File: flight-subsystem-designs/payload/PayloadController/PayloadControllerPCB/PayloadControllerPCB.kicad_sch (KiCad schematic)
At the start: 2 parts

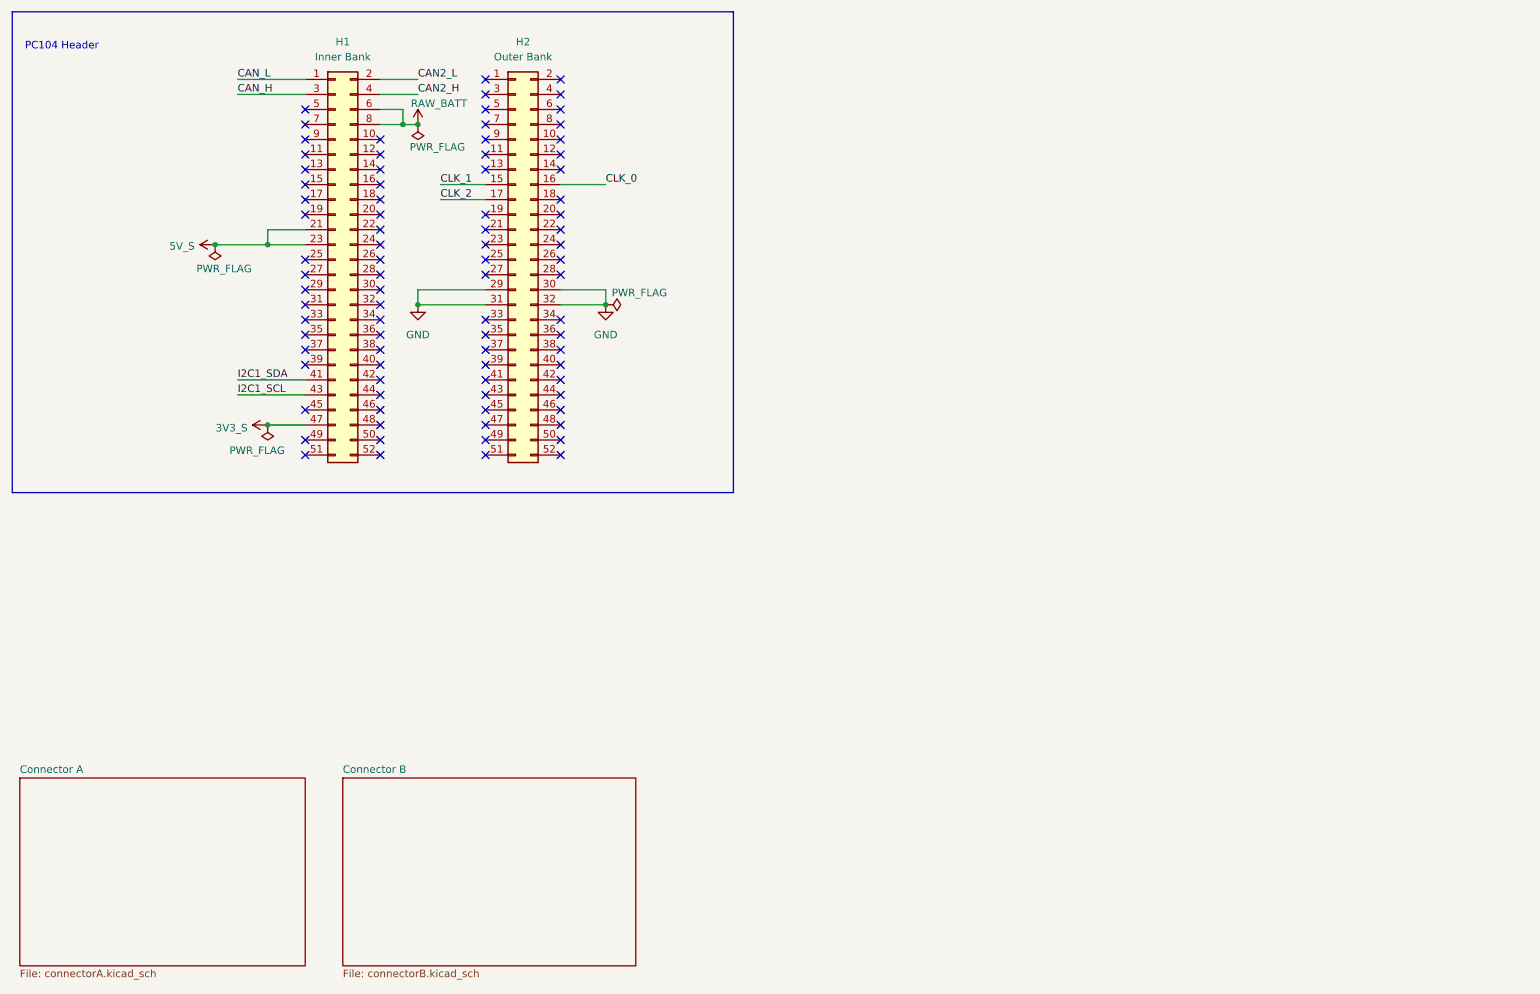
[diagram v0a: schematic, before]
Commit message: Update PC104 schematic
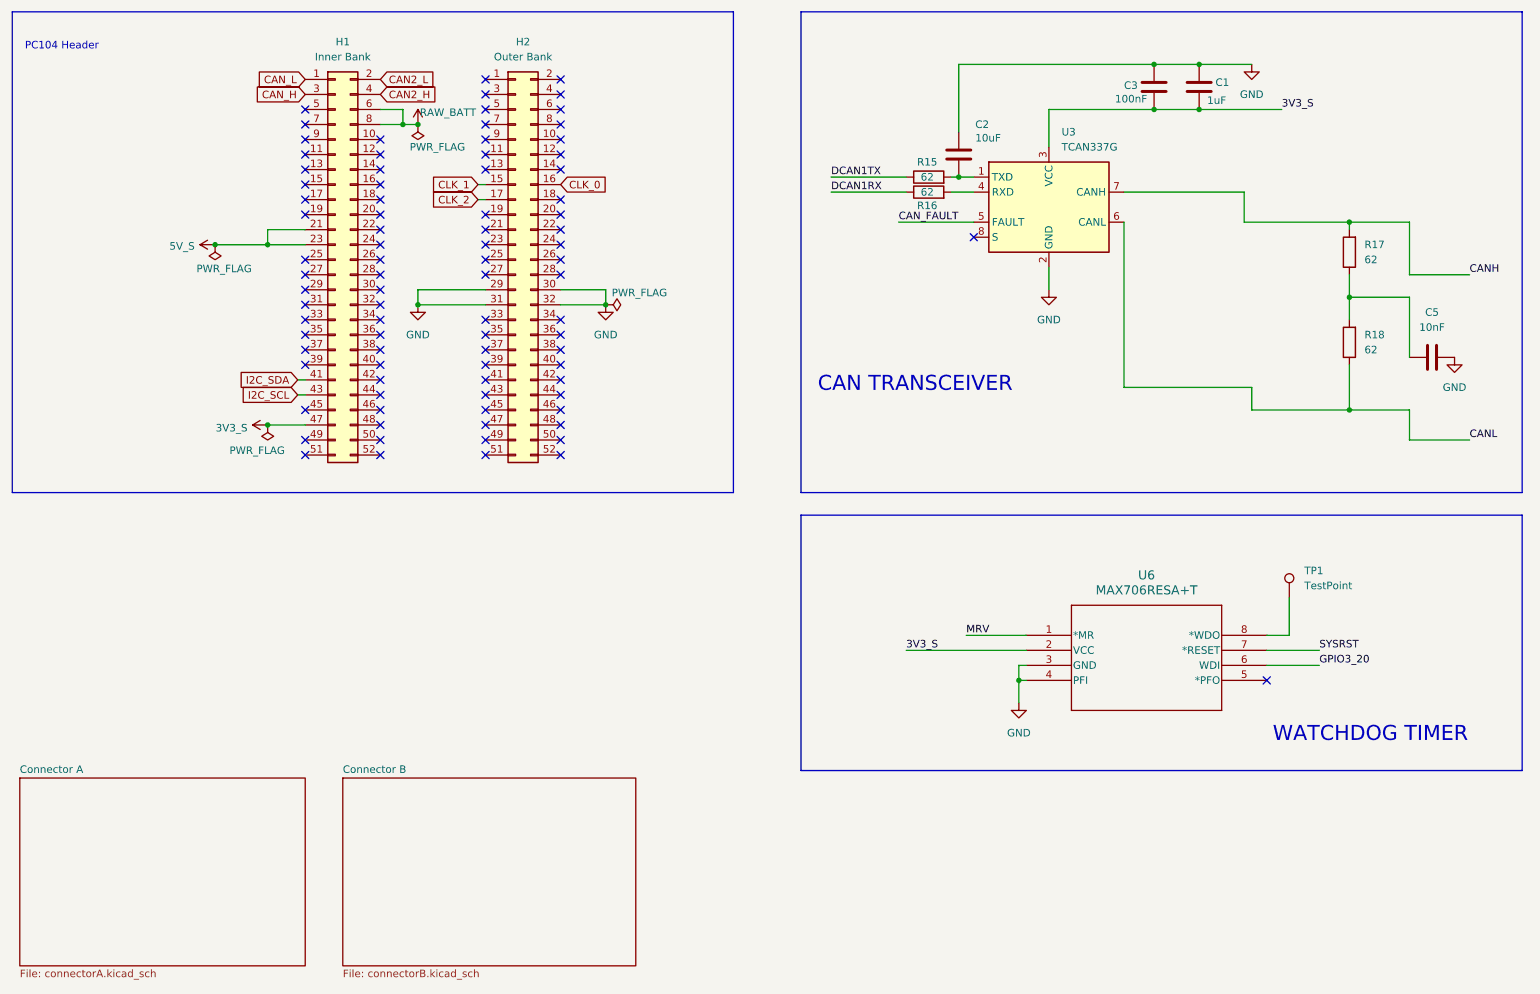
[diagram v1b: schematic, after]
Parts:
- added C1: 1uF, Capacitor_SMD:C_0805_2012Metric_Pad1.18x1.45mm_HandSolder, symbol Device:C
- added C2: 10uF, Capacitor_SMD:C_0805_2012Metric_Pad1.18x1.45mm_HandSolder, symbol Device:C
- added C3: 100nF, Capacitor_SMD:C_0805_2012Metric_Pad1.18x1.45mm_HandSolder, symbol Device:C
- added C5: 10nF, Capacitor_SMD:C_0805_2012Metric_Pad1.18x1.45mm_HandSolder, symbol Device:C
- added R15, R16, R17, R18: 62, Resistor_SMD:R_0805_2012Metric_Pad1.20x1.40mm_HandSolder, symbol Device:R
- added TP1: TestPoint, TestPoint:TestPoint_THTPad_D3.0mm_Drill1.5mm, symbol Connector:TestPoint
- added U3: TCAN337G, Package_TO_SOT_SMD:TSOT-23-8, symbol Interface_CAN_LIN:TCAN337G
- added U6: MAX706RESA+T, 21-0041B_8_MXM, symbol 2026-01-20_01-46-08:MAX706RESA+T
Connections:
- net 3V3_S: now also C1.1, C3.1, U3.3 (VCC), U6.2 (VCC)
- net GND: now also C1.2, C2.1, C3.2, C5.2, U3.2 (GND), U6.3 (GND), U6.4 (PFI)
- net I2C1_SCL renamed I2C_SCL
- net I2C1_SDA renamed I2C_SDA
- new net: C2.2, R15.2, U3.1 (TXD)
- new net: R16.2, U3.4 (RXD)
- new net: C5.1, R17.1, R18.2
- new net: TP1.1, U6.8 (*WDO)
- new net CANH: R17.2, U3.7 (CANH)
- new net CANL: R18.1, U3.6 (CANL)
- new net CAN_FAULT: U3.5 (FAULT)
- new net DCAN1RX: R16.1
- new net DCAN1TX: R15.1
- new net GPIO3_20: U6.6 (WDI)
- new net MRV: U6.1 (*MR)
- new net SYSRST: U6.7 (*RESET)
- no-connect marks 86 -> 88
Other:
- note added: "CAN TRANSCEIVER"
- note added: "WATCHDOG TIMER"

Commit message: Update PLCL schematic
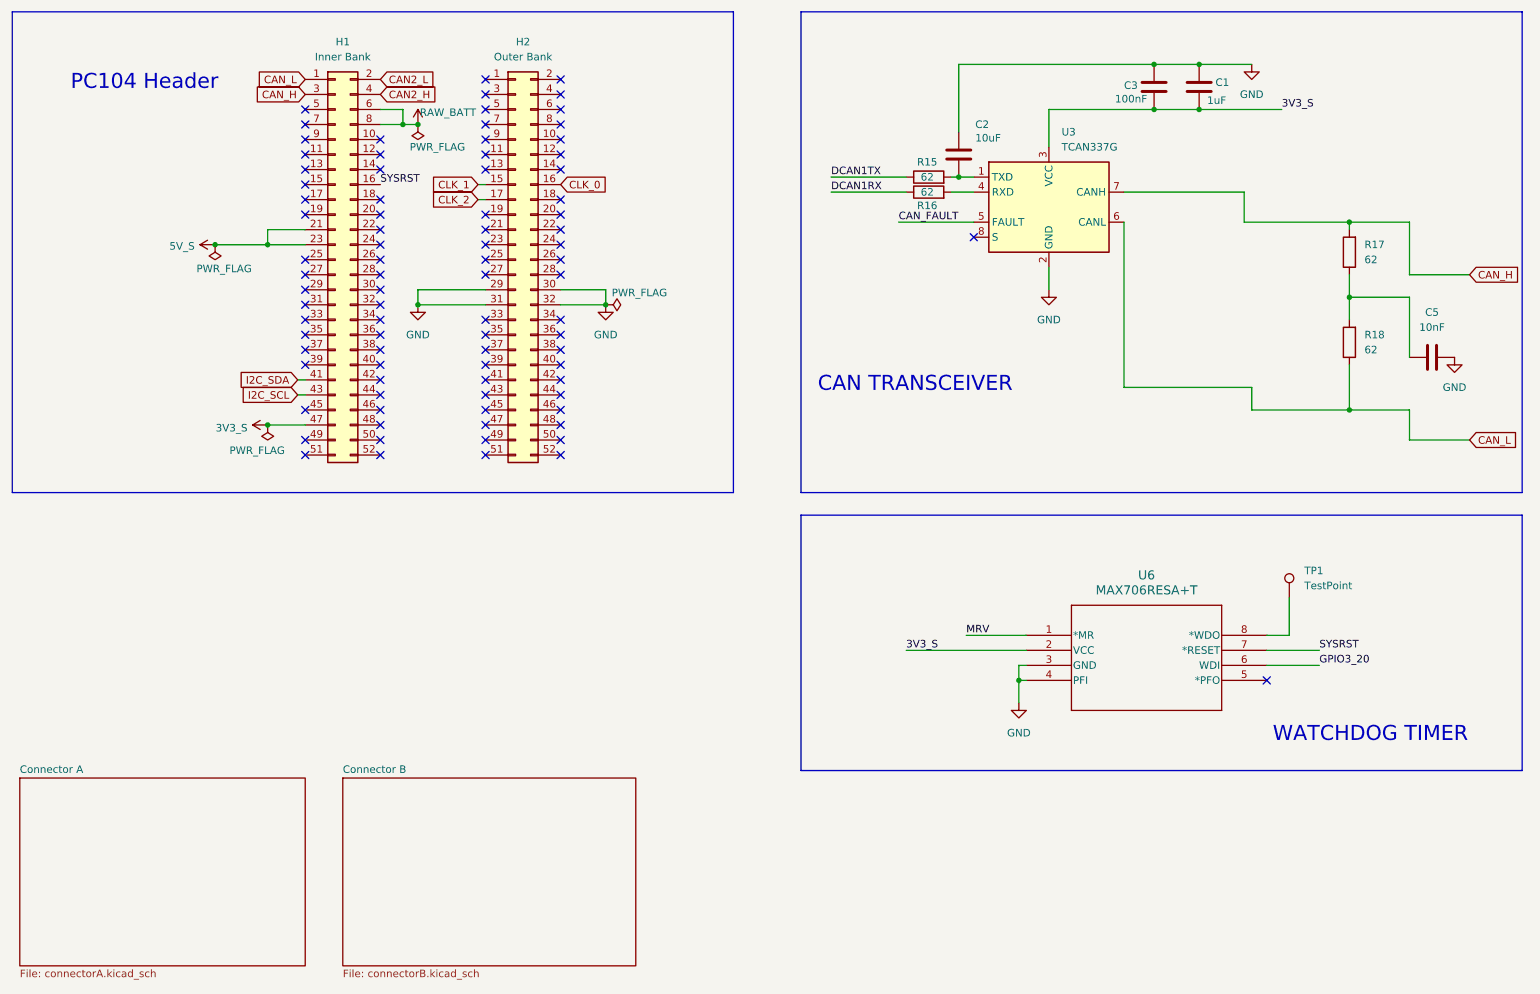
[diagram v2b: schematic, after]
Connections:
- net CANH is gone; now on net CAN_H: R17.2, U3.7 (CANH)
- net CANL is gone; now on net CAN_L: R18.1, U3.6 (CANL)
- net SYSRST: now also H1.16 (Pin_16)
- no-connect marks 88 -> 87
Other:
- company: (none) -> UChicago Space Program
- title: (none) -> Payload Controller
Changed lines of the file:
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@@
 	(generator_version "9.0")
 	(paper "A4")
+	(title_block
+		(title "Payload Controller")
+		(rev "1.0")
+		(company "UChicago Space Program")
+	)
 	(rectangle
 		(start 156.21 26.67)
@@
 	(text "PC104 Header\n"
 		(exclude_from_sim no)
-		(at 31.242 32.512 0)
-		(effects
-			(font
-				(size 1.27 1.27)
+		(at 45.212 38.608 0)
+		(effects
+			(font
+				(size 2.54 2.54)
 			)
 		)
@@
 	)
 	(no_connect
-		(at 85.09 55.88)
-	)
-	(no_connect
 		(at 102.87 96.52)
 	)
@@
 		)
 	)
-	(label "CANL"
-		(at 269.24 99.06 0)
-		(effects
-			(font
-				(size 1.27 1.27)
-			)
-			(justify left bottom)
-		)
-	)
-	(label "CANH"
-		(at 269.24 71.12 0)
+	(label "SYSRST"
+		(at 85.09 55.88 0)
 		(effects
 			(font
@@
 		)
 	)
+	(global_label "CAN_H"
+		(shape input)
+		(at 269.24 71.12 0)
+		(fields_autoplaced yes)
+		(effects
+			(font
+				(size 1.27 1.27)
+			)
+			(justify left)
+		)
+		(property "Intersheetrefs" "${INTERSHEET_REFS}"
+			(at 278.2124 71.12 0)
+			(effects
+				(font
+					(size 1.27 1.27)
+				)
+				(justify left)
+				(hide yes)
+			)
+		)
+	)
 	(global_label "CLK_2"
 		(shape input)
@@
 				(hide yes)
 			)
+		)
+	)
+	(global_label "CAN_L"
+		(shape input)
+		(at 269.24 99.06 0)
+		(fields_autoplaced yes)
+		(effects
+			(font
+				(size 1.27 1.27)
+			)
+			(justify left)
+		)
+		(property "Intersheetrefs" "${INTERSHEET_REFS}"
+			(at 277.91 99.06 0)
+			(effects
+				(font
+					(size 1.27 1.27)
+				)
+				(justify left)
+				(hide yes)
+			)

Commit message: Update PLCL Schematic
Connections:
- net RS45B: now reaches H1.11 (Pin_11)
- net RS45A: now reaches H1.9 (Pin_9)
- net I2C_SCL: no longer names the net of H1.43 (Pin_43)
- net I2C_SDA: no longer names the net of H1.41 (Pin_41)
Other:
- added sheet Payload Connectors (payload_connectors.kicad_sch)
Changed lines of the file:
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@@
 	)
 	(no_connect
+		(at 71.12 88.9)
+	)
+	(no_connect
 		(at 115.57 81.28)
 	)
@@
 	)
 	(no_connect
-		(at 72.39 50.8)
+		(at 102.87 66.04)
 	)
 	(no_connect
-		(at 102.87 66.04)
+		(at 71.12 91.44)
 	)
 	(no_connect
@@
 	)
 	(no_connect
-		(at 72.39 48.26)
-	)
-	(no_connect
 		(at 72.39 73.66)
 	)
@@
 		)
 	)
-	(global_label "CAN_L"
+	(global_label "RS45A"
 		(shape input)
-		(at 269.24 99.06 0)
+		(at 72.39 48.26 180)
 		(fields_autoplaced yes)
 		(effects
@@
 				(size 1.27 1.27)
 			)
-			(justify left)
+			(justify right)
 		)
 		(property "Intersheetrefs" "${INTERSHEET_REFS}"
-			(at 277.91 99.06 0)
+			(at 63.4177 48.26 0)
 			(effects
 				(font
 					(size 1.27 1.27)
 				)
-				(justify left)
+				(justify right)
 				(hide yes)
 			)
 		)
 	)
-	(global_label "CLK_0"
+	(global_label "CAN_L"
 		(shape input)
-		(at 115.57 55.88 0)
+		(at 269.24 99.06 0)
 		(fields_autoplaced yes)
 		(effects
@@
 		)
 		(property "Intersheetrefs" "${INTERSHEET_REFS}"
-			(at 124.3004 55.88 0)
+			(at 277.91 99.06 0)
 			(effects
 				(font
@@
 		)
 	)
-	(global_label "I2C_SDA"
+	(global_label "CLK_0"
 		(shape input)
-		(at 71.12 88.9 180)
+		(at 115.57 55.88 0)
 		(fields_autoplaced yes)
 		(effects
@@
 				(size 1.27 1.27)
 			)
-			(justify right)
+			(justify left)
 		)
 		(property "Intersheetrefs" "${INTERSHEET_REFS}"
-			(at 60.5148 88.9 0)
+			(at 124.3004 55.88 0)
 			(effects
 				(font
 					(size 1.27 1.27)
 				)
-				(justify right)
+				(justify left)
 				(hide yes)
 			)
 		)
 	)
-	(global_label "I2C_SCL"
+	(global_label "CLK_1"
 		(shape input)
-		(at 71.12 91.44 180)
+		(at 101.6 55.88 180)
 		(fields_autoplaced yes)
 		(effects
@@
 		)
 		(property "Intersheetrefs" "${INTERSHEET_REFS}"
-			(at 60.5753 91.44 0)
+			(at 92.8696 55.88 0)
 			(effects
 				(font
@@
 		)
 	)
-	(global_label "CLK_1"
+	(global_label "RS45B"
 		(shape input)
-		(at 101.6 55.88 180)
+		(at 72.39 50.8 180)
 		(fields_autoplaced yes)
 		(effects
@@
 		)
 		(property "Intersheetrefs" "${INTERSHEET_REFS}"
-			(at 92.8696 55.88 0)
+			(at 63.2363 50.8 0)
 			(effects
 				(font
@@
 	)
 	(symbol
-		(lib_name "+3.3V_1")
 		(lib_id "power:+3.3V")
 		(at 57.15 66.04 90)
@@
 	)
 	(sheet
-		(at 24.13 156.21)
+		(at 22.86 114.3)
 		(size 48.26 31.75)
 		(exclude_from_sim no)
@@
 		)
 		(property "Sheetname" "Connector A"
-			(at 24.13 155.4984 0)
+			(at 22.86 113.5884 0)
 			(effects
 				(font
@@
 		)
 		(property "Sheetfile" "connectorA.kicad_sch"
-			(at 24.13 188.5446 0)
+			(at 22.86 146.6346 0)
 			(effects
 				(font
@@
 	)
 	(sheet
-		(at 78.74 156.21)
+		(at 76.2 114.3)
 		(size 49.53 31.75)
 		(exclude_from_sim no)
@@
 		)
 		(property "Sheetname" "Connector B"
-			(at 78.74 155.4984 0)
+			(at 76.2 113.5884 0)
 			(effects
 				(font
@@
 		)
 		(property "Sheetfile" "connectorB.kicad_sch"
-			(at 78.74 188.5446 0)
+			(at 76.2 146.6346 0)
 			(effects
 				(font
@@
 				)
 			)
+		)
+	)
+	(sheet
+		(at 22.86 154.94)
+		(size 49.53 31.75)
+		(exclude_from_sim no)
+		(in_bom yes)
+		(on_board yes)
+		(dnp no)
+		(fields_autoplaced yes)
+		(stroke
+			(width 0.1524)
+			(type solid)
+		)
+		(fill
+			(color 0 0 0 0.0000)
+		)
+		(property "Sheetname" "Payload Connectors"
+			(at 22.86 154.2284 0)
+			(effects
+				(font
+					(size 1.27 1.27)
+				)
+				(justify left bottom)
+			)
+		)
+		(property "Sheetfile" "payload_connectors.kicad_sch"
+			(at 22.86 187.2746 0)
+			(effects
+				(font
+					(size 1.27 1.27)
+				)
+				(justify left top)
+			)
+		)
+		(instances
+			(project "PayloadControllerPCB"
+				(path "/ab286999-0fbe-469b-b161-54b65f8cdf9b"
+					(page "4")
+				)
+			)
